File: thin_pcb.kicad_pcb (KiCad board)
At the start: 2 copper layers, 95.2 x 95.2 mm, 190 parts, among them J01 Conn_01x02, J02 Conn_01x02, J04 Conn_01x02, J06 Conn_01x02, J07 Conn_01x02, J08 Conn_01x02, J1 USB_B_Micro, J11 Conn_01x03, J12 Conn_01x03, J13 Conn_01x03, J14 Conn_01x03, J15 Conn_01x03, J16 Conn_01x03, J17 Conn_01x03, J18 Conn_01x03, J2 AudioJack4_Ground, J21 Conn_01x07, J22 Conn_01x07, J23 Conn_01x07, J24 Conn_01x07, J25 Conn_01x07, J26 Conn_01x07, J27 Conn_01x07, J28 Conn_01x07, J3 AudioJack4_Ground, J31 Conn_01x07, J32 Conn_01x07, J33 Conn_01x07, J34 Conn_01x07, J35 Conn_01x07, J36 Conn_01x07, J37 Conn_01x07, J38 Conn_01x07, J4 Conn_01x06, J41 Conn_01x04, J42 Conn_01x04, J43 Conn_01x04, J44 Conn_01x04, J45 Conn_01x04, J46 Conn_01x04, J47 Conn_01x04, J48 Conn_01x04, J5 Conn_01x06, J51 Conn_01x01, J52 Conn_01x01, J53 Conn_01x01, J54 Conn_01x01, J55 Conn_01x01, J56 Conn_01x01, J57 Conn_01x01, J58 Conn_01x01, J6 Conn_02x02, J7 Conn_01x02, SW11 SW_Push, SW12 SW_Push, SW13 SW_Push, SW14 SW_Push, SW15 SW_Push, SW21 SW_Push, SW22 SW_Push, SW23 SW_Push, SW24 SW_Push, SW25 SW_Push, SW252 SW_Push, SW31 SW_Push, SW32 SW_Push, SW33 SW_Push, SW34 SW_Push, SW35 SW_Push, SW41 SW_Push, SW42 SW_Push, SW422 SW_Push, SW43 SW_Push, SW44 SW_Push, SW45 SW_Push, SW452 SW_Push, SW51 SW_Push, SW52 SW_Push, SW522 SW_Push, SW53 SW_Push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

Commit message: aligning
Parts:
- removed the ? at (105.4, 81.9) (x2)
- added ? (x2): , , F.Cu at (105.4, 81.9)

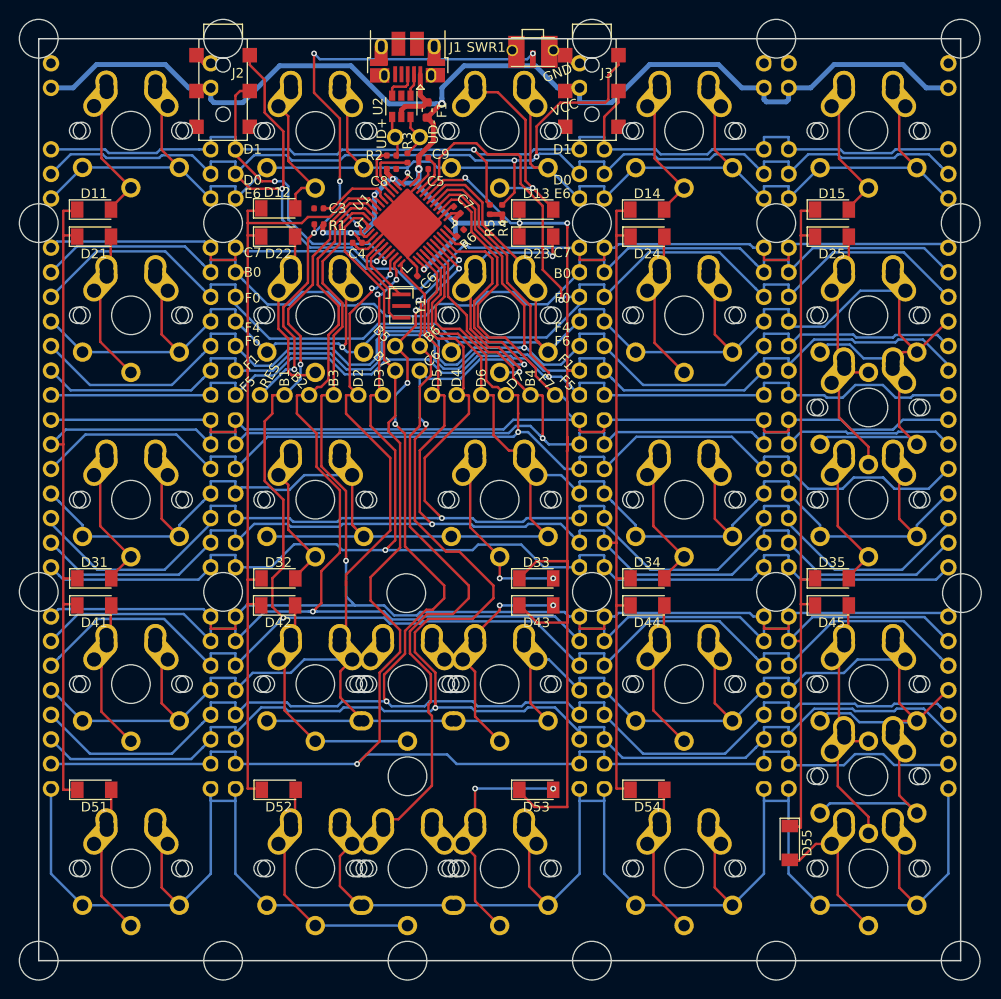
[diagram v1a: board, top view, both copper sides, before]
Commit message: pcb class 0.2
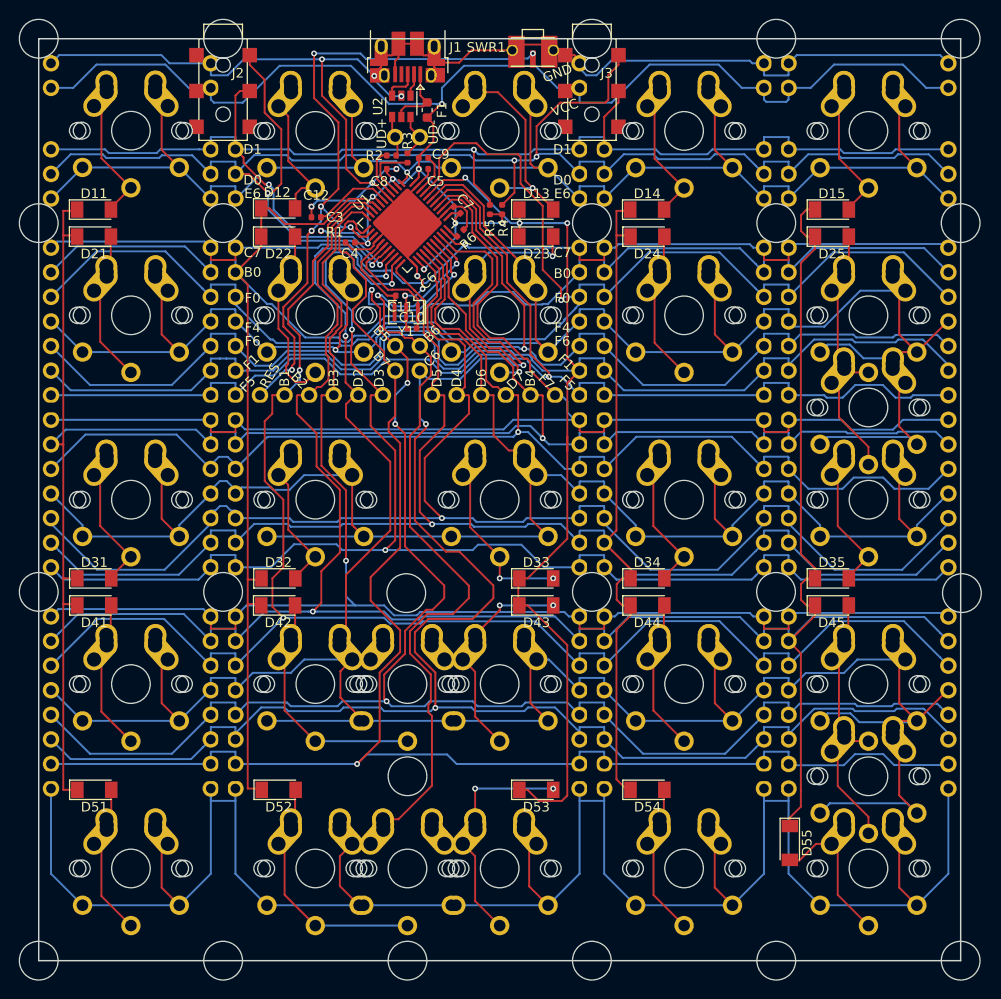
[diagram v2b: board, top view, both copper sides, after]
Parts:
- removed the ? at (105.4, 81.9) (x2)
- added ? (x2): , , F.Cu at (105.4, 81.9)
- added C10: 10p, Capacitor_SMD:C_0402_1005Metric, F.Cu at (90.0, 89.0)
- added C11: 10p, Capacitor_SMD:C_0402_1005Metric, F.Cu at (88.8, 85.6)
- added C12: 100u, Capacitor_SMD:C_0402_1005Metric, F.Cu at (80.1, 76.4)
- moved C3 0.96 mm to (80.1, 77.5)
- moved Y1 0.80 mm to (89.4, 87.3), turned to 180 degrees
- moved C4 0.74 mm to (83.6, 80.1)
- moved R1 0.72 mm to (80.1, 78.9)
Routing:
- net GND: track 32.9 -> 186.6 mm, vias 0 -> 9
- net D3: track 140.0 -> 152.6 mm
- net D2: track 238.4 -> 249.0 mm
- net F1: track 221.6 -> 212.5 mm
- net B5: track 167.9 -> 176.5 mm
- net B6: track 289.3 -> 297.3 mm
- net XTAL1: track 7.01 -> 12.9 mm
- net B0: track 195.9 -> 193.9 mm
- net B7: track 169.0 -> 170.4 mm
- net D6: track 191.6 -> 190.6 mm
- net F0: track 150.1 -> 151.2 mm
- net D7: track 137.3 -> 136.3 mm
- net Net-(D22-Pad2): track 15.2 -> 16.2 mm
- net D1: track 146.5 -> 145.6 mm
- net D0: track 168.0 -> 168.8 mm
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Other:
- net class Default: clearance 0.127 -> 0.2; trace_width 0.254 -> 0.2
- net class Power: clearance 0.1905 -> 0.2; trace_width 0.508 -> 0.2; via_dia 0.8 -> 0.6; via_drill 0.4 -> 0.3
- rule trace_clearance: 0.127 -> 0.2
- rule trace_min: 0.127 -> 0.2
- rule via_min_drill: 0.2 -> 0.3
- rule via_min_size: 0.3 -> 0.6

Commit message: column pins
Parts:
- removed the ? at (105.4, 81.9) (x2)
- added ? (x2): , , F.Cu at (105.4, 81.9)
- added J111: Conn_01x01, lib:PinSocket_1x01_P2.54mm_Vertical, F.Cu at (55.2, 60.3)
- added J115: Conn_01x01, lib:PinSocket_1x01_P2.54mm_Vertical, F.Cu at (131.4, 60.3)
- added J121: Conn_01x01, lib:PinSocket_1x01_P2.54mm_Vertical, F.Cu at (55.2, 79.4)
- added J124: Conn_01x01, lib:PinSocket_1x01_P2.54mm_Vertical, F.Cu at (112.4, 79.4)
- added J125: Conn_01x01, lib:PinSocket_1x01_P2.54mm_Vertical, F.Cu at (131.4, 79.4)
- added J131: Conn_01x01, lib:PinSocket_1x01_P2.54mm_Vertical, F.Cu at (55.2, 98.4)
- added J132: Conn_01x01, lib:PinSocket_1x01_P2.54mm_Vertical, F.Cu at (74.3, 98.4)
- added J133: Conn_01x01, lib:PinSocket_1x01_P2.54mm_Vertical, F.Cu at (104.8, 98.4)
- added J134: Conn_01x01, lib:PinSocket_1x01_P2.54mm_Vertical, F.Cu at (112.4, 98.4)
- added J141: Conn_01x01, lib:PinSocket_1x01_P2.54mm_Vertical, F.Cu at (55.2, 117.5)
- added J142: Conn_01x01, lib:PinSocket_1x01_P2.54mm_Vertical, F.Cu at (74.3, 117.5)
- added J143: Conn_01x01, lib:PinSocket_1x01_P2.54mm_Vertical, F.Cu at (104.8, 117.5)
- added J144: Conn_01x01, lib:PinSocket_1x01_P2.54mm_Vertical, F.Cu at (112.4, 117.5)
- added J145: Conn_01x01, lib:PinSocket_1x01_P2.54mm_Vertical, F.Cu at (131.4, 117.5)
- added J151: Conn_01x01, lib:PinSocket_1x01_P2.54mm_Vertical, F.Cu at (55.2, 136.5)
- added J152: Conn_01x01, lib:PinSocket_1x01_P2.54mm_Vertical, F.Cu at (74.3, 136.5)
- added J153: Conn_01x01, lib:PinSocket_1x01_P2.54mm_Vertical, F.Cu at (104.8, 136.5)
- added J154: Conn_01x01, lib:PinSocket_1x01_P2.54mm_Vertical, F.Cu at (112.4, 136.5)
- added J211: Conn_01x01, lib:PinSocket_1x01_P2.54mm_Vertical, F.Cu at (55.2, 76.8)
- added J214: Conn_01x01, lib:PinSocket_1x01_P2.54mm_Vertical, F.Cu at (112.4, 76.8)
- added J215: Conn_01x01, lib:PinSocket_1x01_P2.54mm_Vertical, F.Cu at (131.4, 76.8)
- added J221: Conn_01x01, lib:PinSocket_1x01_P2.54mm_Vertical, F.Cu at (55.2, 95.9)
- added J224: Conn_01x01, lib:PinSocket_1x01_P2.54mm_Vertical, F.Cu at (112.4, 95.9)
- added J231: Conn_01x01, lib:PinSocket_1x01_P2.54mm_Vertical, F.Cu at (55.2, 114.9)
- added J232: Conn_01x01, lib:PinSocket_1x01_P2.54mm_Vertical, F.Cu at (74.3, 114.9)
- added J233: Conn_01x01, lib:PinSocket_1x01_P2.54mm_Vertical, F.Cu at (104.8, 114.9)
- added J234: Conn_01x01, lib:PinSocket_1x01_P2.54mm_Vertical, F.Cu at (112.4, 114.9)
- added J235: Conn_01x01, lib:PinSocket_1x01_P2.54mm_Vertical, F.Cu at (131.4, 114.9)
- added J241: Conn_01x01, lib:PinSocket_1x01_P2.54mm_Vertical, F.Cu at (55.2, 134.0)
- added J242: Conn_01x01, lib:PinSocket_1x01_P2.54mm_Vertical, F.Cu at (74.3, 134.0)
- added J243: Conn_01x01, lib:PinSocket_1x01_P2.54mm_Vertical, F.Cu at (104.8, 134.0)
- added J244: Conn_01x01, lib:PinSocket_1x01_P2.54mm_Vertical, F.Cu at (112.4, 134.0)
- added J251: Conn_01x01, lib:PinSocket_1x01_P2.54mm_Vertical, F.Cu at (55.2, 153.0)
- added J252: Conn_01x01, lib:PinSocket_1x01_P2.54mm_Vertical, F.Cu at (74.3, 153.0)
- added J253: Conn_01x01, lib:PinSocket_1x01_P2.54mm_Vertical, F.Cu at (104.8, 153.0)
- added J254: Conn_01x01, lib:PinSocket_1x01_P2.54mm_Vertical, F.Cu at (112.4, 153.0)
- added J255: Conn_01x01, lib:PinSocket_1x01_P2.54mm_Vertical, F.Cu at (131.4, 153.0)
- moved D21 2.57 mm to (59.7, 79.5)
- moved D31 2.54 mm to (59.7, 114.8)
- moved D41 2.54 mm to (59.7, 117.6)
- moved D51 2.54 mm to (59.7, 136.7)
- moved D11 2.51 mm to (59.7, 76.7)
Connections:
- J11 pad 3: E6 -> D5
- J12 pad 3: E6 -> D5
- J13 pad 3: E6 -> D5
- J14 pad 3: E6 -> D5
- J15 pad 3: E6 -> D5
- J16 pad 3: E6 -> D5
- J17 pad 3: E6 -> D5
- J18 pad 3: E6 -> D5
- J21 pad 4: F4 -> D5
- J22 pad 4: F4 -> D5
- J23 pad 4: F4 -> D5
- J24 pad 4: F4 -> D5
- J25 pad 4: F4 -> D5
- J26 pad 4: F4 -> D5
- J27 pad 4: F4 -> D5
- J28 pad 4: F4 -> D5
- J31 pad 4: D6 -> D5
- J32 pad 4: D6 -> D5
- J33 pad 4: D6 -> D5
- J34 pad 4: D6 -> D5
- J35 pad 4: D6 -> D5
- J36 pad 4: D6 -> D5
- J37 pad 4: D6 -> D5
- J38 pad 4: D6 -> D5
- J5 pad 3: D6 -> D5
- SW11 pad 2: E6 -> D5
- SW12 pad 2: E6 -> D5
- SW13 pad 2: E6 -> D5
- SW14 pad 2: E6 -> D5
- SW15 pad 2: E6 -> D5
- SW21 pad 2: F4 -> D5
- SW22 pad 2: F4 -> D5
- SW23 pad 2: F4 -> D5
- SW24 pad 2: F4 -> D5
- SW25 pad 2: F4 -> D5
- SW252 pad 2: F4 -> D5
- SW31 pad 2: D6 -> D5
- SW32 pad 2: D6 -> D5
- SW33 pad 2: D6 -> D5
- SW34 pad 2: D6 -> D5
- SW35 pad 2: D6 -> D5
- U1 pad 1: E6 -> D5
- U1 pad 26: D6 -> D5
- U1 pad 39: F4 -> D5
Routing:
- net D5: track 210.6 -> 747.4 mm, vias 1 -> 3
- net F4: track 197.1 -> 0.00 mm, vias 1 -> 0
- net D6: track 190.6 -> 0.00 mm
- net E6: track 150.8 -> 0.00 mm, vias 1 -> 0
- net B4: track 199.5 -> 253.2 mm
- net Net-(D51-Pad2): track 13.3 -> 15.1 mm
- net Net-(D41-Pad2): track 13.9 -> 15.8 mm
- net Net-(D21-Pad2): track 13.5 -> 15.3 mm
- net D1: track 145.6 -> 144.5 mm
- net C7: track 108.2 -> 107.1 mm
- net F0: track 151.2 -> 150.1 mm
- net F5: track 135.0 -> 133.9 mm
- net F6: track 139.1 -> 138.2 mm
- net Net-(D11-Pad2): track 13.3 -> 12.5 mm
- net D0: track 168.8 -> 168.0 mm
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
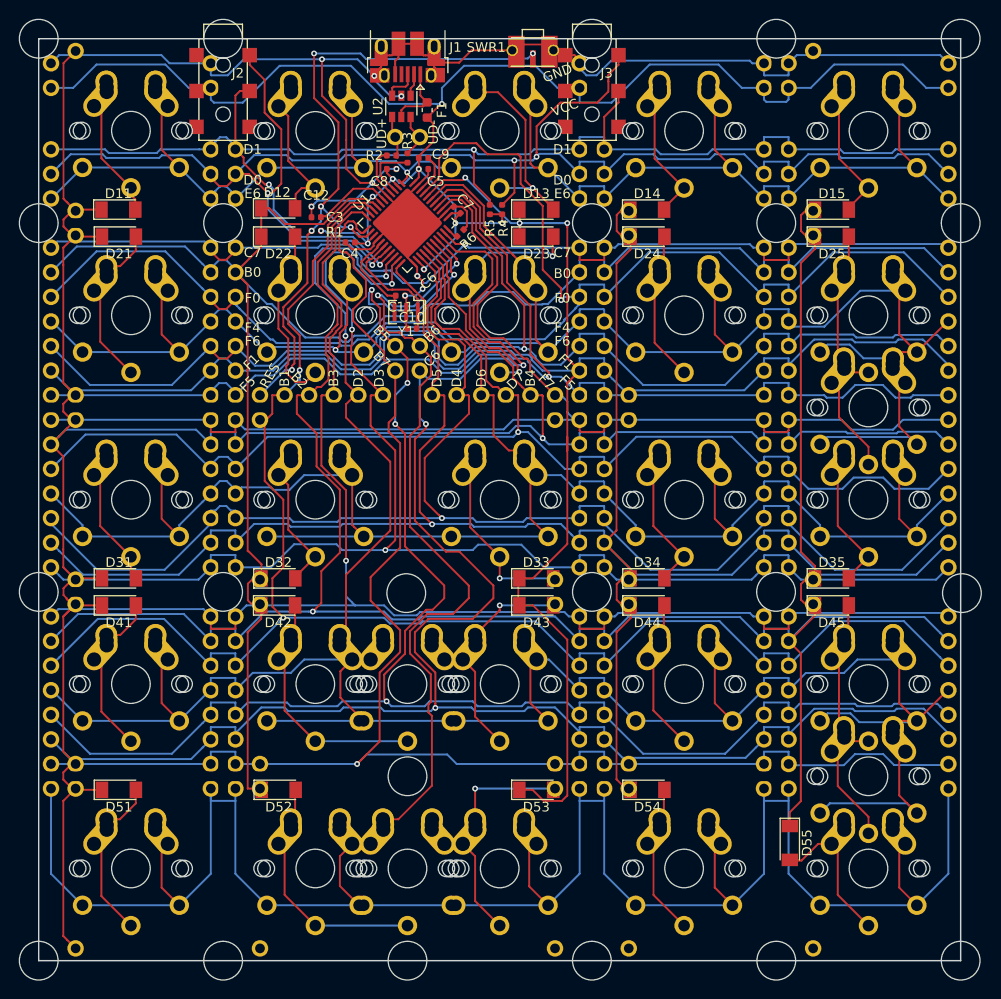
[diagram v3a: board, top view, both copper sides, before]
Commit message: remove 90 angles
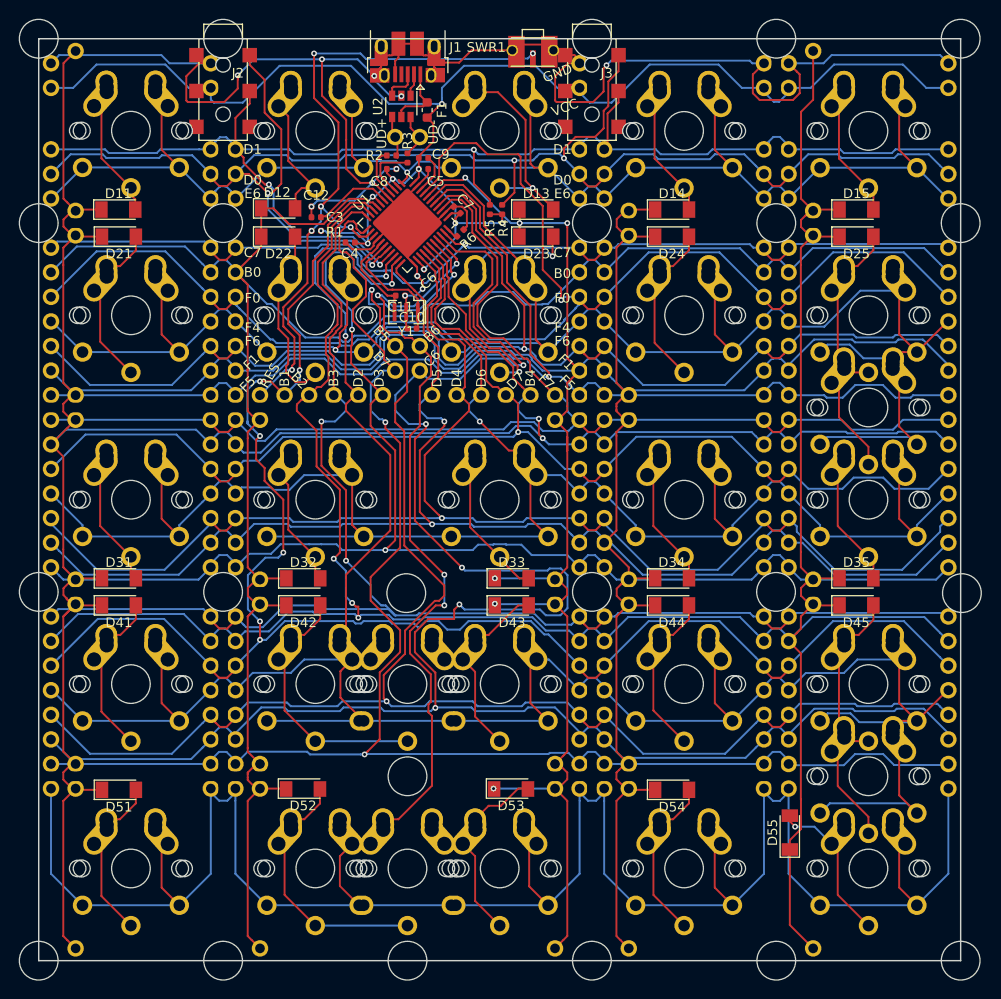
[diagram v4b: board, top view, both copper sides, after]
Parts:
- removed the ? at (105.4, 81.9) (x2)
- added ? (x2): , , F.Cu at (105.4, 81.9)
- moved D53 2.61 mm to (100.2, 136.5)
- moved D42 2.60 mm to (78.8, 117.6)
- moved D14 2.57 mm to (116.9, 76.7)
- moved D32 2.57 mm to (78.8, 114.8)
- moved D15 2.54 mm to (135.9, 76.7)
- moved D25 2.54 mm to (135.9, 79.5)
- moved D35 2.54 mm to (135.9, 114.8)
- moved D45 2.54 mm to (135.9, 117.6)
- moved D24 2.54 mm to (116.9, 79.5)
- moved D33 2.54 mm to (100.3, 114.8)
- moved D34 2.54 mm to (116.9, 114.8)
- moved D43 2.54 mm to (100.3, 117.6)
- moved D44 2.54 mm to (116.9, 117.6)
- moved D54 2.54 mm to (116.9, 136.7)
- moved D52 2.52 mm to (78.7, 136.5)
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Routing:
- net B2: track 233.3 -> 272.1 mm, vias 1 -> 3
- net F1: track 212.1 -> 239.9 mm, vias 3 -> 6
- net D5: track 747.4 -> 774.5 mm, vias 3 -> 5
- net B0: track 193.3 -> 219.8 mm
- net GND: track 186.6 -> 213.0 mm, vias 9 -> 11
- net C6: track 191.5 -> 209.5 mm, vias 3 -> 5
- net B1: track 169.0 -> 176.2 mm, vias 2 -> 6
- net Net-(D53-Pad2): track 21.3 -> 16.8 mm, vias 2 -> 0
- net D0: track 168.0 -> 163.9 mm
- net Net-(D33-Pad2): track 17.8 -> 14.0 mm, vias 2 -> 0
- net D3: track 152.6 -> 149.1 mm
- net B5: track 176.5 -> 173.1 mm, vias 5 -> 3
- net D2: track 249.0 -> 245.8 mm
- net D4: track 150.7 -> 147.8 mm
- net B3: track 150.6 -> 153.4 mm, vias 1 -> 2
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
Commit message: breakline & vcc
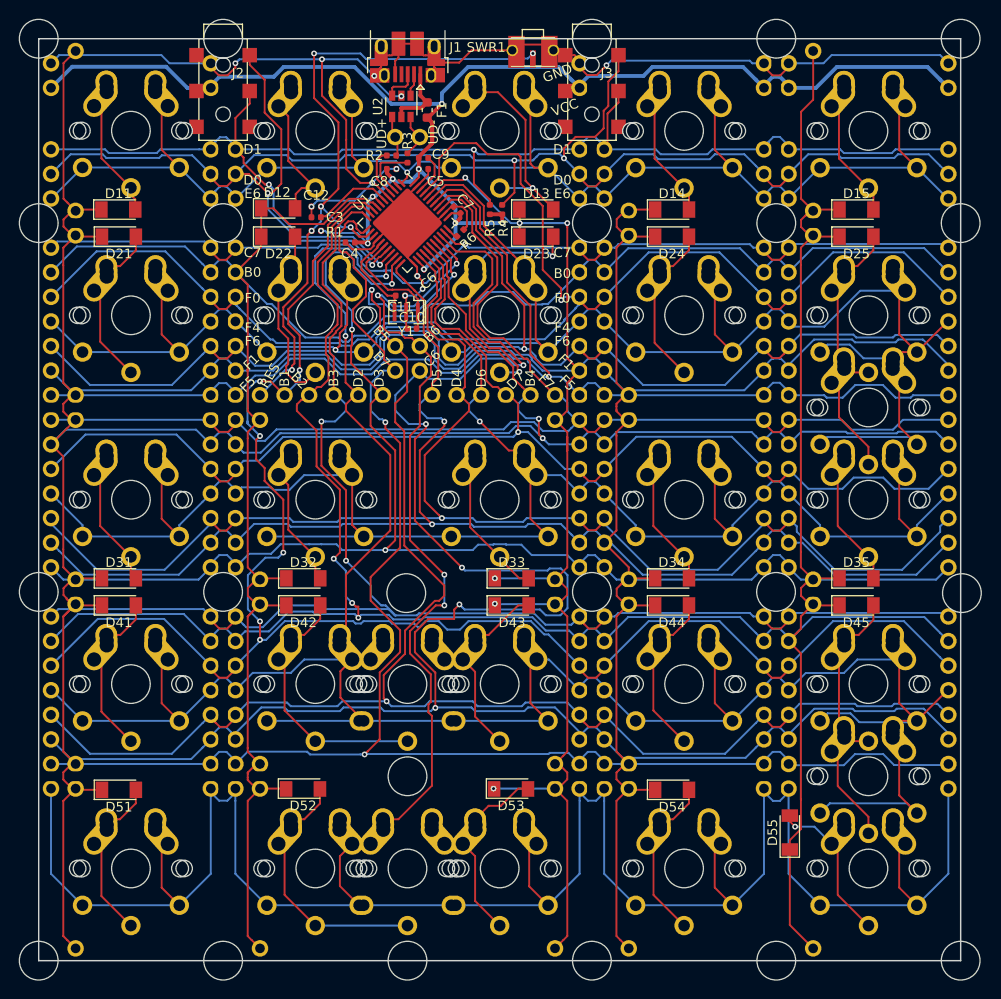
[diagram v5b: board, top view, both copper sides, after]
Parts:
- removed the ? at (105.4, 81.9) (x2)
- removed the REF** at (127.6, 64.1)
- removed the REF** at (108.6, 98.4)
- removed the REF** at (127.6, 98.4)
- removed the REF** at (127.6, 80.6)
- removed the REF** at (70.5, 64.1)
- removed the REF** at (108.6, 64.1)
- removed the REF** at (108.6, 67.9)
- removed the REF** at (70.5, 67.9)
- removed the REF** at (92.1, 97.2)
- removed the REF** at (127.6, 61.6)
- removed the REF** at (127.6, 67.9)
- removed the REF** at (70.5, 80.6)
- removed the REF** at (70.5, 98.4)
- removed the REF** at (70.5, 118.7)
- removed the REF** at (127.6, 118.7)
- removed the REF** at (108.6, 118.7)
- added ? (x2): , , F.Cu at (105.4, 81.9)
- added REF**: BreakLine_2_4_4_4, lib:BreakLine_2_4_4_4, F.Cu at (107.3, 97.2)
- added REF**: BreakLine_2_4_4_2_2, lib:BreakLine_2_4_4_2_2, F.Cu at (70.5, 118.7)
- added REF**: BreakLine_2_4_4_2_2, lib:BreakLine_2_4_4_2_2, F.Cu at (70.5, 80.6)
- added REF**: BreakLine_2_4_5_2, lib:BreakLine_2_4_5_2, F.Cu at (127.6, 75.6)
- added REF**: BreakLine_2_4_5, lib:BreakLine_2_4_5, F.Cu at (108.6, 75.5)
- added REF**: BreakLine_2_4_5, lib:BreakLine_2_4_5, F.Cu at (70.5, 75.6)
- added REF**: BreakLine_2_4_4_2_2, lib:BreakLine_2_4_4_2_2, F.Cu at (70.5, 98.4)
- added REF**: BreakLine_2_4_4_2_2, lib:BreakLine_2_4_4_2_2, F.Cu at (127.6, 118.7)
- added REF**: BreakLine_2_4_4_2_2, lib:BreakLine_2_4_4_2_2, F.Cu at (108.6, 118.7)
- added REF**: BreakLine_2_4_4_2_2, lib:BreakLine_2_4_4_2_2, F.Cu at (108.6, 98.4)
- added REF**: BreakLine_2_4_4_2_2, lib:BreakLine_2_4_4_2_2, F.Cu at (127.6, 98.4)
- added REF**: BreakLine_2_4_4_2_2, lib:BreakLine_2_4_4_2_2, F.Cu at (127.6, 80.6)
- REF** (x2): value BreakLine_2x7 -> BreakLine_2_4_4_2_2; footprint lib:BreakLine_2x7 -> lib:BreakLine_2_4_4_2_2
- REF**: value BreakLine_2x7 -> BreakLine_2_12.16_2; footprint lib:BreakLine_2x7 -> lib:BreakLine_2_12.16_2
- REF**: value BreakLine_2x7 -> BreakLine_2_8_2_2; footprint lib:BreakLine_2x7 -> lib:BreakLine_2_8_2_2
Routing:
- net GND: track 213.0 -> 185.3 mm
- net VCC: track 170.5 -> 171.9 mm
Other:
- net class Power: trace_width 0.2 -> 0.4

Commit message: bug fixes
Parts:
- removed the ? at (105.4, 81.9) (x2)
- added ? (x2): , , F.Cu at (105.4, 81.9)
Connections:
- J11 pad 3: D5 -> E6
- J12 pad 3: D5 -> E6
- J13 pad 3: D5 -> E6
- J14 pad 3: D5 -> E6
- J15 pad 3: D5 -> E6
- J16 pad 3: D5 -> E6
- J17 pad 3: D5 -> E6
- J18 pad 3: D5 -> E6
- J21 pad 4: D5 -> F4
- J22 pad 4: D5 -> F4
- J23 pad 4: D5 -> F4
- J24 pad 4: D5 -> F4
- J25 pad 4: D5 -> F4
- J26 pad 4: D5 -> F4
- J27 pad 4: D5 -> F4
- J28 pad 4: D5 -> F4
- J31 pad 4: D5 -> D6
- J32 pad 4: D5 -> D6
- J33 pad 4: D5 -> D6
- J34 pad 4: D5 -> D6
- J35 pad 4: D5 -> D6
- J36 pad 4: D5 -> D6
- J37 pad 4: D5 -> D6
- J38 pad 4: D5 -> D6
- J5 pad 3: D5 -> D6
- SW11 pad 2: D5 -> E6
- SW12 pad 2: D5 -> E6
- SW13 pad 2: D5 -> E6
- SW14 pad 2: D5 -> E6
- SW15 pad 2: D5 -> E6
- SW21 pad 2: D5 -> F4
- SW22 pad 2: D5 -> F4
- SW23 pad 2: D5 -> F4
- SW24 pad 2: D5 -> F4
- SW25 pad 2: D5 -> F4
- SW252 pad 2: D5 -> F4
- SW31 pad 2: D5 -> D6
- SW32 pad 2: D5 -> D6
- SW33 pad 2: D5 -> D6
- SW34 pad 2: D5 -> D6
- SW35 pad 2: D5 -> D6
- U1 pad 1: D5 -> E6
- U1 pad 26: D5 -> D6
- U1 pad 39: D5 -> F4
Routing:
- net D5: track 774.5 -> 244.3 mm, vias 5 -> 2
- net F4: track 0.00 -> 194.6 mm, vias 0 -> 1
- net D6: track 0.00 -> 189.3 mm, vias 0 -> 1
- net E6: track 0.00 -> 147.7 mm, vias 0 -> 1
- net D7: track 133.9 -> 138.8 mm
- net B4: track 252.3 -> 257.1 mm
- net B7: track 168.7 -> 172.1 mm
- net B6: track 297.4 -> 295.0 mm
- net B5: track 173.1 -> 170.8 mm
- net F7: track 134.9 -> 137.0 mm
- net F5: track 131.8 -> 133.7 mm
- net D4: track 147.8 -> 148.6 mm
- net B3: track 153.4 -> 154.1 mm
- net D0: track 163.9 -> 164.5 mm
